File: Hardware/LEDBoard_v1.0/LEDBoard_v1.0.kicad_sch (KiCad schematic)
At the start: 4 parts, among them J1 Conn_01x02, SW1 SW_Push

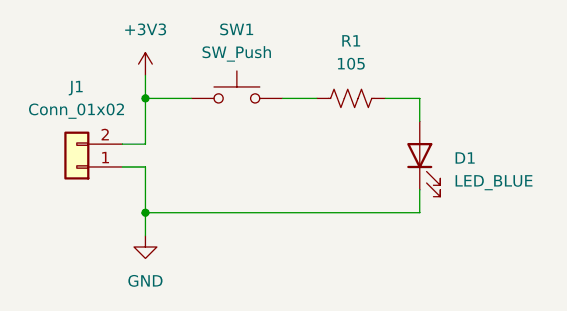
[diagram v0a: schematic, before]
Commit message: fix power flag
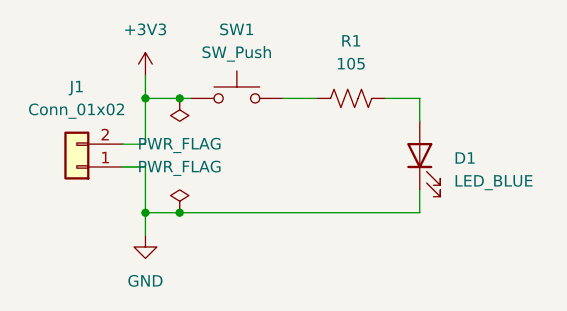
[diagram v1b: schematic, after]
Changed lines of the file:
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@@
+	)
+	(junction
+		(at 53.34 66.04)
+		(diameter 0)
+		(color 0 0 0 0)
 	)
 	(junction
@@
 		(color 0 0 0 0)
 	)
+	(junction
+		(at 53.34 53.34)
+		(diameter 0)
+		(color 0 0 0 0)
+	)
 	(wire
 		(pts
@@
 	(wire
 		(pts
-			(xy 49.53 66.04) (xy 80.01 66.04)
+			(xy 49.53 66.04) (xy 53.34 66.04)
 		)
 		(stroke
@@
 	(wire
 		(pts
-			(xy 49.53 53.34) (xy 54.61 53.34)
+			(xy 53.34 66.04) (xy 80.01 66.04)
+		)
+		(stroke
+			(width 0)
+			(type default)
+		)
+	)
+	(wire
+		(pts
+			(xy 49.53 53.34) (xy 53.34 53.34)
 		)
 		(stroke
@@
 		(pts
 			(xy 49.53 60.96) (xy 49.53 66.04)
+		)
+		(stroke
+			(width 0)
+			(type default)
+		)
+	)
+	(wire
+		(pts
+			(xy 53.34 53.34) (xy 54.61 53.34)
 		)
 		(stroke
@@
 	)
 	(symbol
+		(lib_id "power:PWR_FLAG")
+		(at 53.34 66.04 0)
+		(unit 1)
+		(exclude_from_sim no)
+		(in_bom yes)
+		(on_board yes)
+		(dnp no)
+		(fields_autoplaced yes)
+		(property "Reference" "#FLG02"
+			(at 53.34 64.135 0)
+			(effects
+				(font
+					(size 1.27 1.27)
+				)
+				(hide yes)
+			)
+		)
+		(property "Value" "PWR_FLAG"
+			(at 53.34 60.96 0)
+			(effects
+				(font
+					(size 1.27 1.27)
+				)
+			)
+		)
+		(property "Footprint" ""
+			(at 53.34 66.04 0)
+			(effects
+				(font
+					(size 1.27 1.27)
+				)
+				(hide yes)
+			)
+		)
+		(property "Datasheet" "~"
+			(at 53.34 66.04 0)
+			(effects
+				(font
+					(size 1.27 1.27)
+				)
+				(hide yes)
+			)
+		)
+		(property "Description" "Special symbol for telling ERC where power comes from"
+			(at 53.34 66.04 0)
+			(effects
+				(font
+					(size 1.27 1.27)
+				)
+				(hide yes)
+			)
+		)
+		(pin "1"
+		)
+		(instances
+			(project ""
+				(path "/1e1b062d-fad0-427c-a622-c5b8a80b5268"
+					(reference "#FLG02")
+					(unit 1)
+				)
+			)
+		)
+	)
+	(symbol
 		(lib_id "Switch:SW_Push")
 		(at 59.69 53.34 0)
@@
 					(unit 1)
 				)
+			)
+		)
+	)
+	(symbol
+		(lib_id "power:PWR_FLAG")
+		(at 53.34 53.34 180)
+		(unit 1)
+		(exclude_from_sim no)
+		(in_bom yes)
+		(on_board yes)
+		(dnp no)
+		(fields_autoplaced yes)
+		(property "Reference" "#FLG01"
+			(at 53.34 55.245 0)
+			(effects
+				(font
+					(size 1.27 1.27)
+				)
+				(hide yes)
+			)
+		)
+		(property "Value" "PWR_FLAG"
+			(at 53.34 58.42 0)
+			(effects
+				(font
+					(size 1.27 1.27)
+				)
+			)
+		)
+		(property "Footprint" ""
+			(at 53.34 53.34 0)
+			(effects
+				(font
+					(size 1.27 1.27)
+				)
+				(hide yes)
+			)
+		)
+		(property "Datasheet" "~"
+			(at 53.34 53.34 0)
+			(effects
+				(font
+					(size 1.27 1.27)
+				)
+				(hide yes)
+			)
+		)
+		(property "Description" "Special symbol for telling ERC where power comes from"
+			(at 53.34 53.34 0)
+			(effects
+				(font
+					(size 1.27 1.27)
+				)
+				(hide yes)
+			)
+		)
+		(pin "1"
+		)
+		(instances
+			(project ""
+				(path "/1e1b062d-fad0-427c-a622-c5b8a80b5268"
+					(reference "#FLG01")
+					(unit 1)
+				)
